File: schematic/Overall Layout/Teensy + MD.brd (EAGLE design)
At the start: 66 x 59.4 mm, 18 parts, among them U2 MAX13054ASA

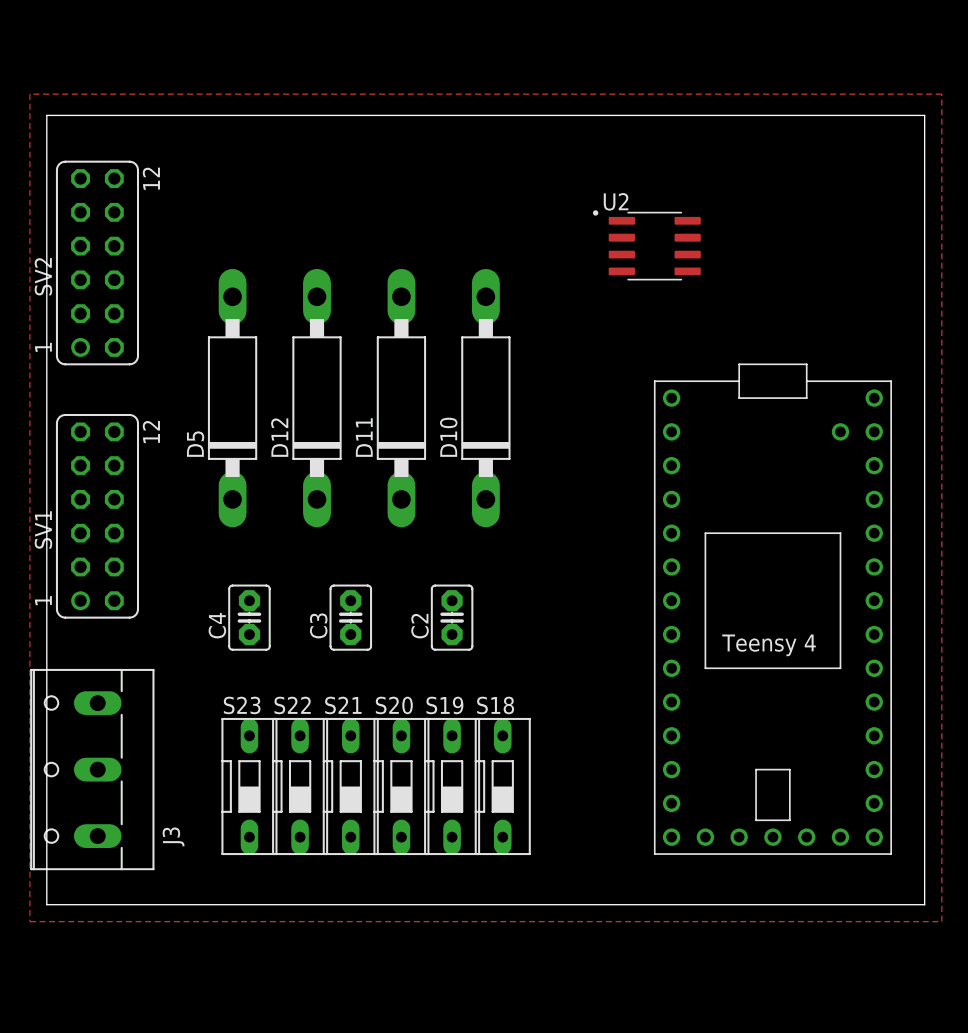
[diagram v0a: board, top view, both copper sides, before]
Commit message: Added military connectors to CAN Bus and added copper threading to PCB designs
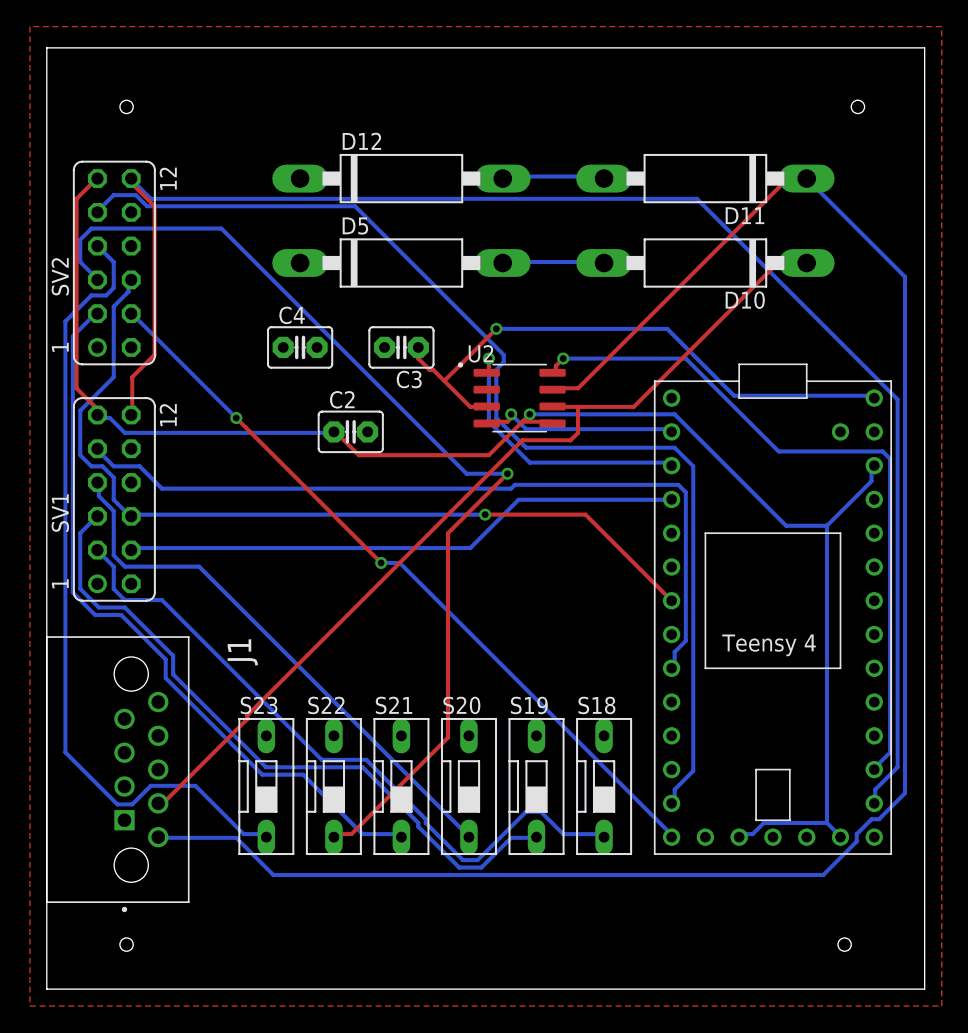
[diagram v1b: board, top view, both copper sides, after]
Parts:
- removed J3: (no value), con-wago-500:W237-103
- added J1: M83513/10-A01NP, M83513_10-A01NP:BEL_M83513/10-A01NP
- moved D11 28.2 mm to (49.5, 54.6), turned to 180 degrees
- moved C3 20.7 mm to (26.7, 41.9), turned to 180 degrees
- moved C4 20.7 mm to (19.1, 41.9), turned to 0 degrees
- moved D10 19.4 mm to (49.5, 48.3), turned to 180 degrees
- moved D12 17.7 mm to (26.7, 54.6), turned to 0 degrees
- moved D5 16.3 mm to (26.7, 48.3), turned to 0 degrees
- moved C2 15.9 mm to (22.9, 35.6), turned to 0 degrees
- moved U2 15.3 mm to (35.6, 38.1)
- moved S18 7.62 mm to (41.9, 8.89)
- moved S19 6.35 mm to (36.8, 8.89)
- moved S20 5.08 mm to (31.8, 8.89)
- moved S21 3.81 mm to (26.7, 8.89)
- moved S22 2.54 mm to (21.6, 8.89)
- moved SV1 1.80 mm to (5.08, 30.5)
- moved S23 1.27 mm to (16.5, 8.89)
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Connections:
- net CAN_BUS: now also J1.6; no longer J3.1
- net GND: now also J1.8; no longer J3.3
- net N$9: now also J1.7; no longer J3.2
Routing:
- net CAN_BUS: track 0.00 -> 135.2 mm
- net +3V3: track 0.00 -> 119.4 mm, vias 0 -> 1
- net MD2.BK: track 0.00 -> 115.1 mm
- net MD2.FR: track 0.00 -> 83.4 mm
- net MD2.X2: track 0.00 -> 77.0 mm, vias 0 -> 1
- net N$9: track 0.00 -> 69.0 mm
- net MD1.5V: track 0.00 -> 64.9 mm, vias 0 -> 1
- net MD2.X1: track 0.00 -> 59.8 mm
- net MD1.FR: track 0.00 -> 59.6 mm
- net MD2.PG: track 0.00 -> 57.0 mm, vias 0 -> 2
- net MD2.X3: track 0.00 -> 55.0 mm
- net N$10: track 0.00 -> 53.0 mm, vias 0 -> 1
- net MD1.X3: track 0.00 -> 51.3 mm
- net MD1.X2: track 0.00 -> 50.9 mm
- net VCC: track 0.00 -> 43.6 mm, vias 0 -> 1
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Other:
- board size 66 x 59.4 mm -> 66 x 70.8 mm
